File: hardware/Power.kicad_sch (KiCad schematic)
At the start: 33 parts, among them J200 Conn_Receptacle_2P, J201 Solder pad, J202 Solder pad, J203 Solder pad, J204 Solder pad, Q200 AO3401A, SW200 SW_Push_Dual, SW201 SW_Push_Dual, SW202 MU-AS90R, U200 RT9080-33GJ5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

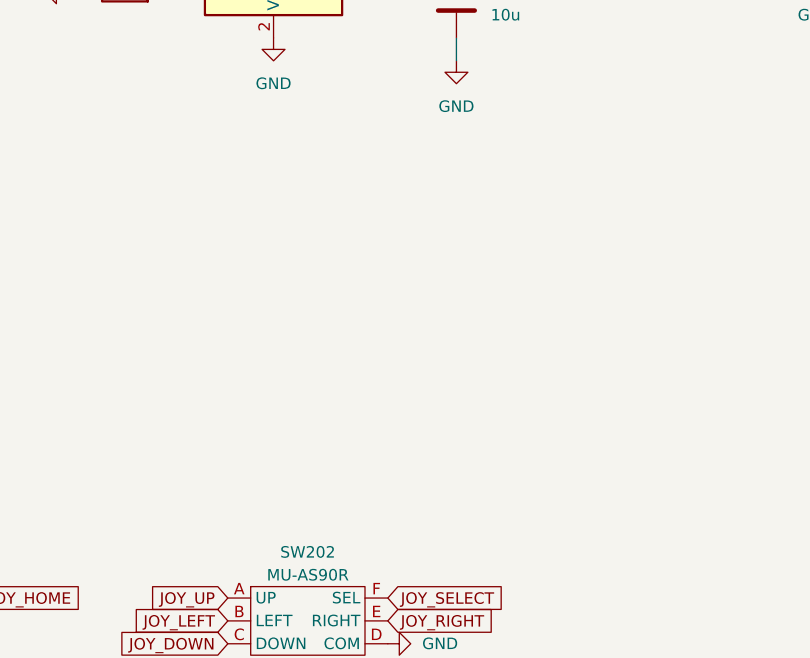
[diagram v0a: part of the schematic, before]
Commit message: Add crystal oscillator and hide designators from PCB
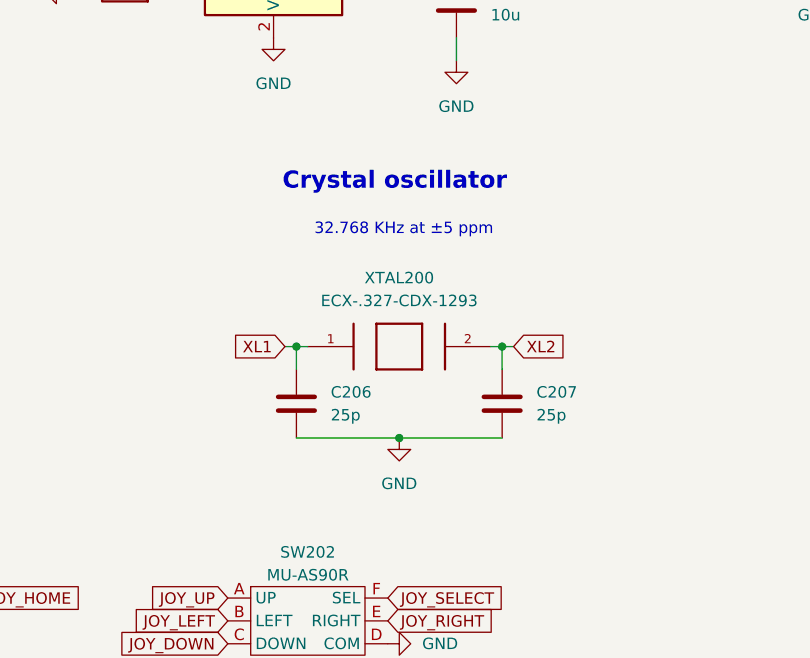
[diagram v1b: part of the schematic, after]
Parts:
- added C206, C207: 25p, Capacitor_SMD:C_0201_0603Metric_Pad0.64x0.40mm_HandSolder, symbol Device:C
- added XTAL200: ECX-.327-CDX-1293, ECX-.327-CDX-1293:XTAL_ECS-.327-12.5-34RR-TR, symbol ECX-.327-CDX-1293:ECX-.327-CDX-1293
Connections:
- net GND: now also C206.2, C207.2
- new net XL1: C206.1, XTAL200.1
- new net XL2: C207.1, XTAL200.2
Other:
- note added: "32.768 KHz at ±5 ppm"
- note added: "Crystal oscillator"

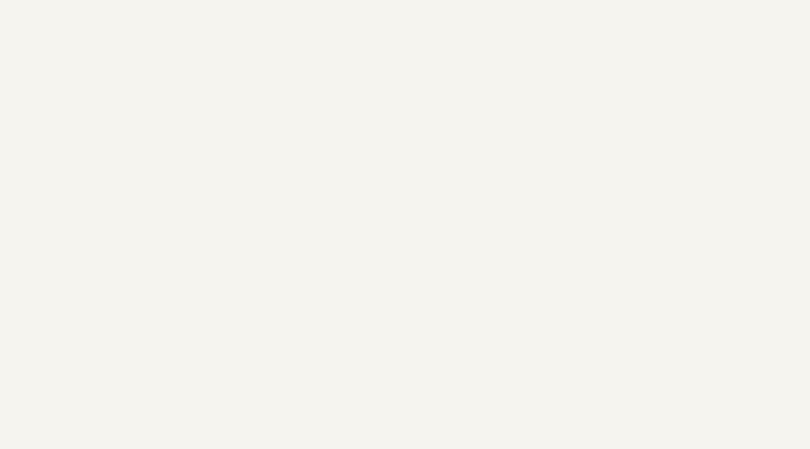
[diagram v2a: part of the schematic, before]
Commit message: Add mounting tabs to edges of PCB
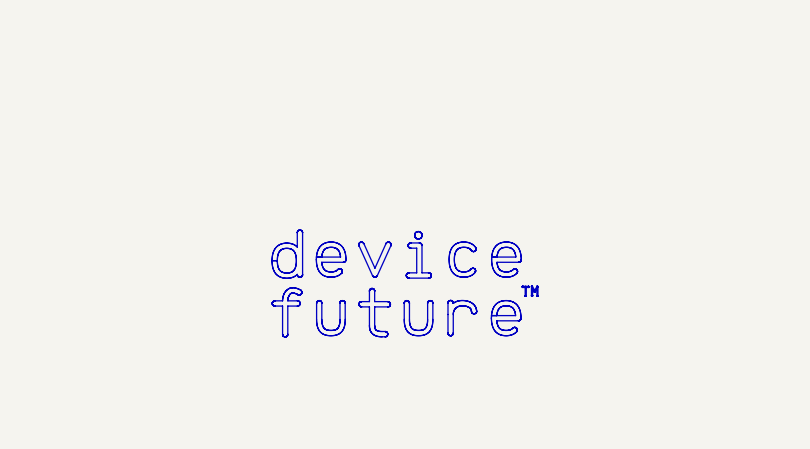
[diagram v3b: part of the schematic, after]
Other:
- company: (none) -> DeviceFuture
- title: (none) -> DigiCron

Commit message: Update PCB to use 0402 resistor/capacitor packages
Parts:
- C200, C201, C202, C203, C204, C205, C206, C207: footprint Capacitor_SMD:C_0201_0603Metric_Pad0.64x0.40mm_HandSolder -> Resistor_SMD:R_0402_1005Metric_Pad0.72x0.64mm_HandSolder
- R200, R201, R202, R203, R204, R205, R206, R207, R208, R209, R210: footprint Resistor_SMD:R_0201_0603Metric_Pad0.64x0.40mm_HandSolder -> Resistor_SMD:R_0402_1005Metric_Pad0.72x0.64mm_HandSolder
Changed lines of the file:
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@@
 			)
 		)
-		(property "Footprint" "Resistor_SMD:R_0201_0603Metric_Pad0.64x0.40mm_HandSolder"
+		(property "Footprint" "Resistor_SMD:R_0402_1005Metric_Pad0.72x0.64mm_HandSolder"
 			(at 123.952 63.5 90)
 			(effects
@@
 			)
 		)
-		(property "Footprint" "Capacitor_SMD:C_0201_0603Metric_Pad0.64x0.40mm_HandSolder"
+		(property "Footprint" "Resistor_SMD:R_0402_1005Metric_Pad0.72x0.64mm_HandSolder"
 			(at 260.35 47.2948 0)
 			(effects
@@
 			)
 		)
-		(property "Footprint" "Capacitor_SMD:C_0201_0603Metric_Pad0.64x0.40mm_HandSolder"
+		(property "Footprint" "Resistor_SMD:R_0402_1005Metric_Pad0.72x0.64mm_HandSolder"
 			(at 252.4252 123.19 0)
 			(effects
@@
 			)
 		)
-		(property "Footprint" "Capacitor_SMD:C_0201_0603Metric_Pad0.64x0.40mm_HandSolder"
+		(property "Footprint" "Resistor_SMD:R_0402_1005Metric_Pad0.72x0.64mm_HandSolder"
 			(at 192.7352 58.42 0)
 			(effects
@@
 			)
 		)
-		(property "Footprint" "Capacitor_SMD:C_0201_0603Metric_Pad0.64x0.40mm_HandSolder"
+		(property "Footprint" "Resistor_SMD:R_0402_1005Metric_Pad0.72x0.64mm_HandSolder"
 			(at 134.3152 120.65 0)
 			(effects
@@
 			)
 		)
-		(property "Footprint" "Resistor_SMD:R_0201_0603Metric_Pad0.64x0.40mm_HandSolder"
+		(property "Footprint" "Resistor_SMD:R_0402_1005Metric_Pad0.72x0.64mm_HandSolder"
 			(at 177.292 54.61 90)
 			(effects
@@
 			)
 		)
-		(property "Footprint" "Capacitor_SMD:C_0201_0603Metric_Pad0.64x0.40mm_HandSolder"
+		(property "Footprint" "Resistor_SMD:R_0402_1005Metric_Pad0.72x0.64mm_HandSolder"
 			(at 173.99 93.0148 0)
 			(effects
@@
 			)
 		)
-		(property "Footprint" "Resistor_SMD:R_0201_0603Metric_Pad0.64x0.40mm_HandSolder"
+		(property "Footprint" "Resistor_SMD:R_0402_1005Metric_Pad0.72x0.64mm_HandSolder"
 			(at 85.09 47.498 90)
 			(effects
@@
 			)
 		)
-		(property "Footprint" "Resistor_SMD:R_0201_0603Metric_Pad0.64x0.40mm_HandSolder"
+		(property "Footprint" "Resistor_SMD:R_0402_1005Metric_Pad0.72x0.64mm_HandSolder"
 			(at 38.1 83.058 90)
 			(effects
@@
 			)
 		)
-		(property "Footprint" "Resistor_SMD:R_0201_0603Metric_Pad0.64x0.40mm_HandSolder"
+		(property "Footprint" "Resistor_SMD:R_0402_1005Metric_Pad0.72x0.64mm_HandSolder"
 			(at 38.1 77.978 90)
 			(effects
@@
 			)
 		)
-		(property "Footprint" "Capacitor_SMD:C_0201_0603Metric_Pad0.64x0.40mm_HandSolder"
+		(property "Footprint" "Resistor_SMD:R_0402_1005Metric_Pad0.72x0.64mm_HandSolder"
 			(at 139.3952 165.1 0)
 			(effects
@@
 			)
 		)
-		(property "Footprint" "Resistor_SMD:R_0201_0603Metric_Pad0.64x0.40mm_HandSolder"
+		(property "Footprint" "Resistor_SMD:R_0402_1005Metric_Pad0.72x0.64mm_HandSolder"
 			(at 241.3 59.182 90)
 			(effects
@@
 			)
 		)
-		(property "Footprint" "Resistor_SMD:R_0201_0603Metric_Pad0.64x0.40mm_HandSolder"
+		(property "Footprint" "Resistor_SMD:R_0402_1005Metric_Pad0.72x0.64mm_HandSolder"
 			(at 224.282 128.27 90)
 			(effects
@@
 			)
 		)
-		(property "Footprint" "Resistor_SMD:R_0201_0603Metric_Pad0.64x0.40mm_HandSolder"
+		(property "Footprint" "Resistor_SMD:R_0402_1005Metric_Pad0.72x0.64mm_HandSolder"
 			(at 96.52 117.348 90)
 			(effects
@@
 			)
 		)
-		(property "Footprint" "Resistor_SMD:R_0201_0603Metric_Pad0.64x0.40mm_HandSolder"
+		(property "Footprint" "Resistor_SMD:R_0402_1005Metric_Pad0.72x0.64mm_HandSolder"
 			(at 123.952 50.8 90)
 			(effects
@@
 			)
 		)
-		(property "Footprint" "Resistor_SMD:R_0201_0603Metric_Pad0.64x0.40mm_HandSolder"
+		(property "Footprint" "Resistor_SMD:R_0402_1005Metric_Pad0.72x0.64mm_HandSolder"
 			(at 224.282 118.11 90)
 			(effects
@@
 			)
 		)
-		(property "Footprint" "Capacitor_SMD:C_0201_0603Metric_Pad0.64x0.40mm_HandSolder"
+		(property "Footprint" "Resistor_SMD:R_0402_1005Metric_Pad0.72x0.64mm_HandSolder"
 			(at 239.7252 123.19 0)
 			(effects
@@
 			)
 		)
-		(property "Footprint" "Capacitor_SMD:C_0201_0603Metric_Pad0.64x0.40mm_HandSolder"
+		(property "Footprint" "Resistor_SMD:R_0402_1005Metric_Pad0.72x0.64mm_HandSolder"
 			(at 116.5352 165.1 0)
 			(effects
@@
 			)
 		)
-		(property "Footprint" "Resistor_SMD:R_0201_0603Metric_Pad0.64x0.40mm_HandSolder"
+		(property "Footprint" "Resistor_SMD:R_0402_1005Metric_Pad0.72x0.64mm_HandSolder"
 			(at 77.47 44.958 90)
 			(effects

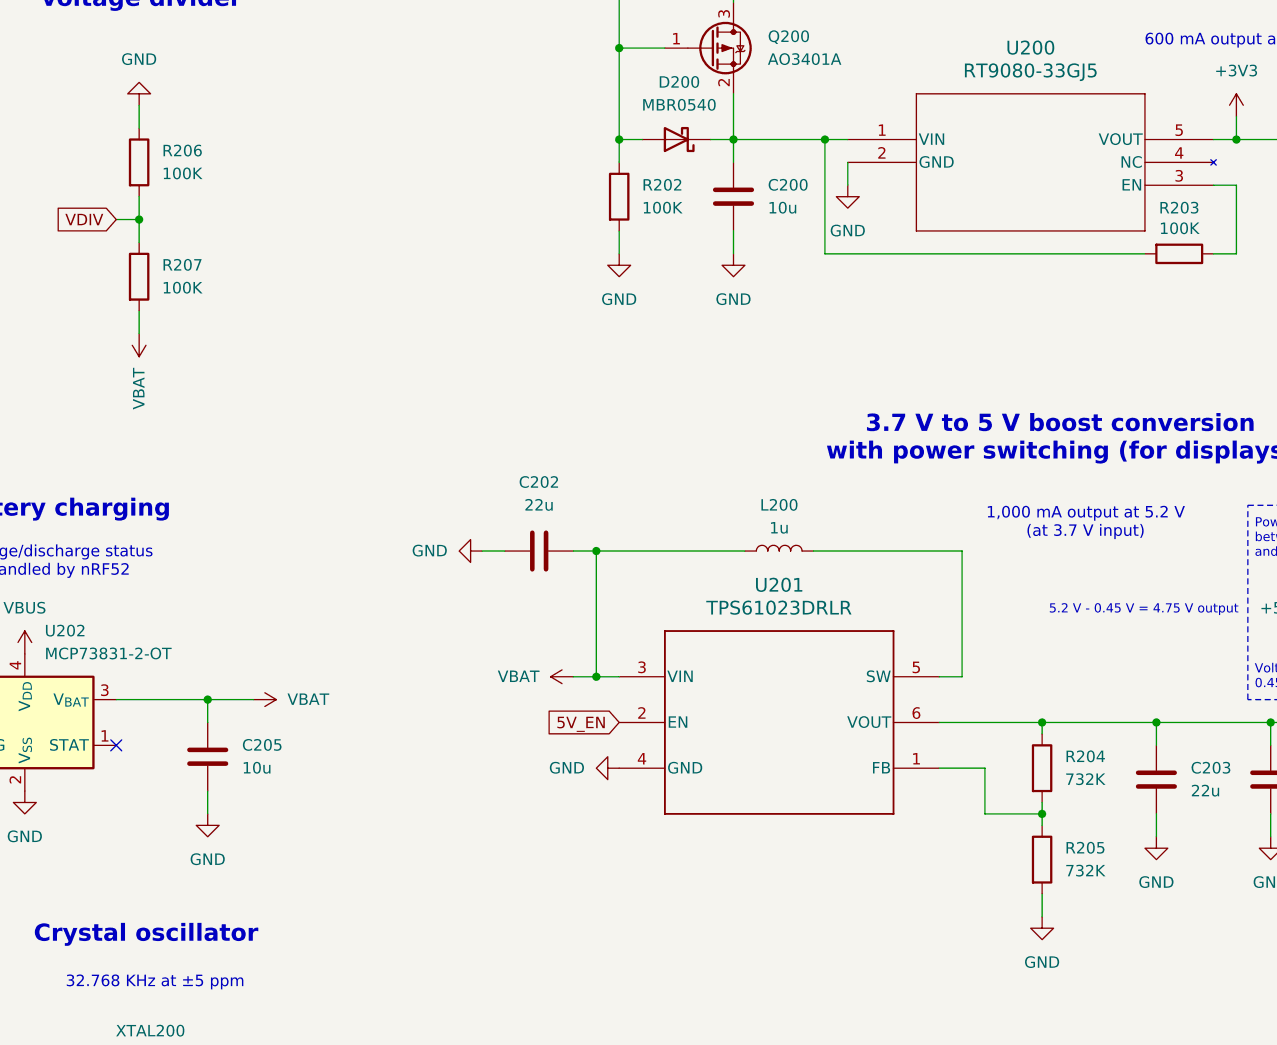
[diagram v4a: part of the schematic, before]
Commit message: Fix a few resistor values on PCB relating to power management
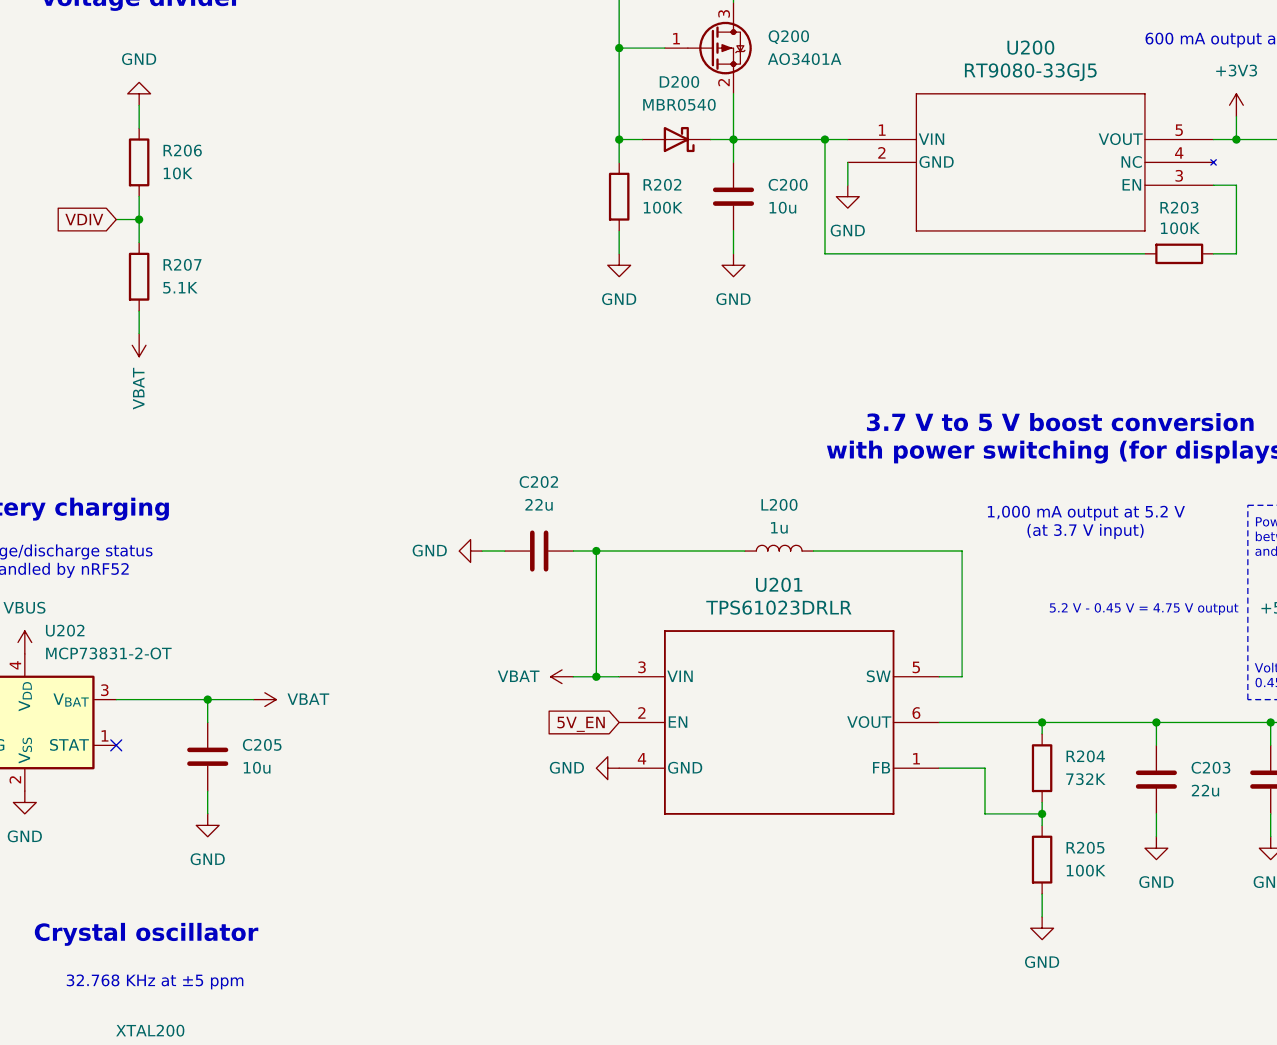
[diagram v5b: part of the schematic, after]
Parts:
- R205: value 732K -> 100K
- R206: value 100K -> 10K
- R207: value 100K -> 5.1K
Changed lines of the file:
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@@
 			)
 		)
-		(property "Value" "100K"
+		(property "Value" "5.1K"
 			(at 128.27 64.7699 0)
 			(effects
@@
 			)
 		)
-		(property "Value" "732K"
+		(property "Value" "100K"
 			(at 228.6 129.5399 0)
 			(effects
@@
 			)
 		)
-		(property "Value" "100K"
+		(property "Value" "10K"
 			(at 128.27 52.0699 0)
 			(effects

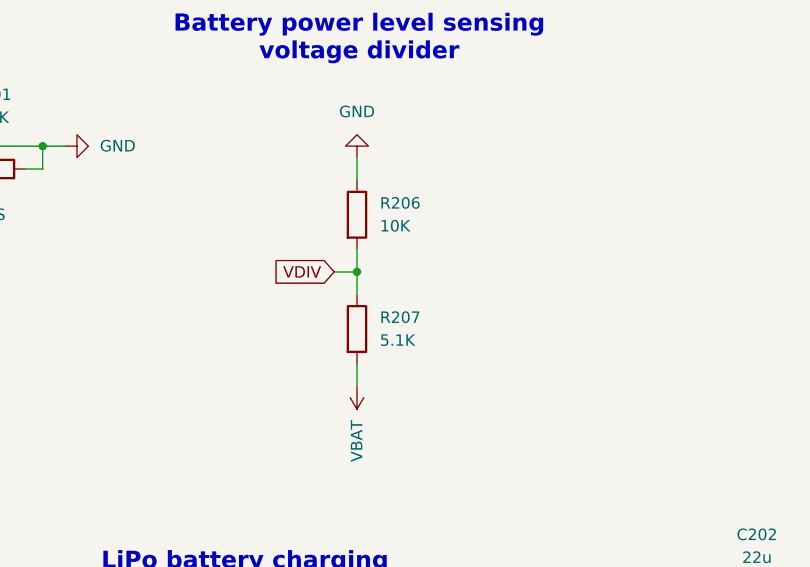
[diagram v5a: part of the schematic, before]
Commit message: Make a few changes to footprint selection and resistor/capacitor values
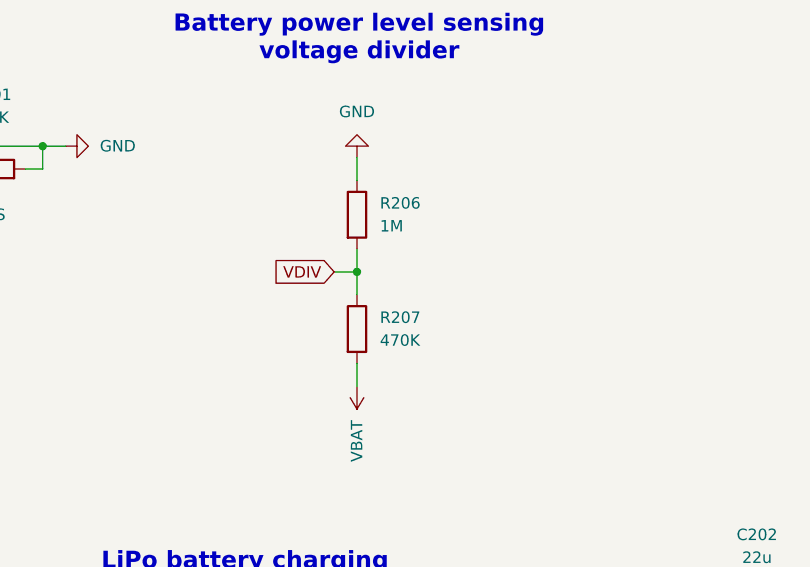
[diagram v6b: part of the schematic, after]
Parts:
- C200, C201, C202, C203, C204, C205, C206, C207: footprint Resistor_SMD:R_0402_1005Metric_Pad0.72x0.64mm_HandSolder -> Capacitor_SMD:C_0402_1005Metric_Pad0.74x0.62mm_HandSolder
- R206: value 10K -> 1M
- R207: value 5.1K -> 470K
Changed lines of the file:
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@@
 			)
 		)
-		(property "Value" "5.1K"
+		(property "Value" "470K"
 			(at 128.27 64.7699 0)
 			(effects
@@
 			)
 		)
-		(property "Footprint" "Resistor_SMD:R_0402_1005Metric_Pad0.72x0.64mm_HandSolder"
+		(property "Footprint" "Capacitor_SMD:C_0402_1005Metric_Pad0.74x0.62mm_HandSolder"
 			(at 260.35 47.2948 0)
 			(effects
@@
 			)
 		)
-		(property "Footprint" "Resistor_SMD:R_0402_1005Metric_Pad0.72x0.64mm_HandSolder"
+		(property "Footprint" "Capacitor_SMD:C_0402_1005Metric_Pad0.74x0.62mm_HandSolder"
 			(at 252.4252 123.19 0)
 			(effects
@@
 			)
 		)
-		(property "Footprint" "Resistor_SMD:R_0402_1005Metric_Pad0.72x0.64mm_HandSolder"
+		(property "Footprint" "Capacitor_SMD:C_0402_1005Metric_Pad0.74x0.62mm_HandSolder"
 			(at 192.7352 58.42 0)
 			(effects
@@
 			)
 		)
-		(property "Footprint" "Resistor_SMD:R_0402_1005Metric_Pad0.72x0.64mm_HandSolder"
+		(property "Footprint" "Capacitor_SMD:C_0402_1005Metric_Pad0.74x0.62mm_HandSolder"
 			(at 134.3152 120.65 0)
 			(effects
@@
 			)
 		)
-		(property "Footprint" "Resistor_SMD:R_0402_1005Metric_Pad0.72x0.64mm_HandSolder"
+		(property "Footprint" "Capacitor_SMD:C_0402_1005Metric_Pad0.74x0.62mm_HandSolder"
 			(at 173.99 93.0148 0)
 			(effects
@@
 			)
 		)
-		(property "Footprint" "Resistor_SMD:R_0402_1005Metric_Pad0.72x0.64mm_HandSolder"
+		(property "Footprint" "Capacitor_SMD:C_0402_1005Metric_Pad0.74x0.62mm_HandSolder"
 			(at 139.3952 165.1 0)
 			(effects
@@
 			)
 		)
-		(property "Value" "10K"
+		(property "Value" "1M"
 			(at 128.27 52.0699 0)
 			(effects
@@
 			)
 		)
-		(property "Footprint" "Resistor_SMD:R_0402_1005Metric_Pad0.72x0.64mm_HandSolder"
+		(property "Footprint" "Capacitor_SMD:C_0402_1005Metric_Pad0.74x0.62mm_HandSolder"
 			(at 239.7252 123.19 0)
 			(effects
@@
 			)
 		)
-		(property "Footprint" "Resistor_SMD:R_0402_1005Metric_Pad0.72x0.64mm_HandSolder"
+		(property "Footprint" "Capacitor_SMD:C_0402_1005Metric_Pad0.74x0.62mm_HandSolder"
 			(at 116.5352 165.1 0)
 			(effects

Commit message: Fix pin routing for battery power level sensing
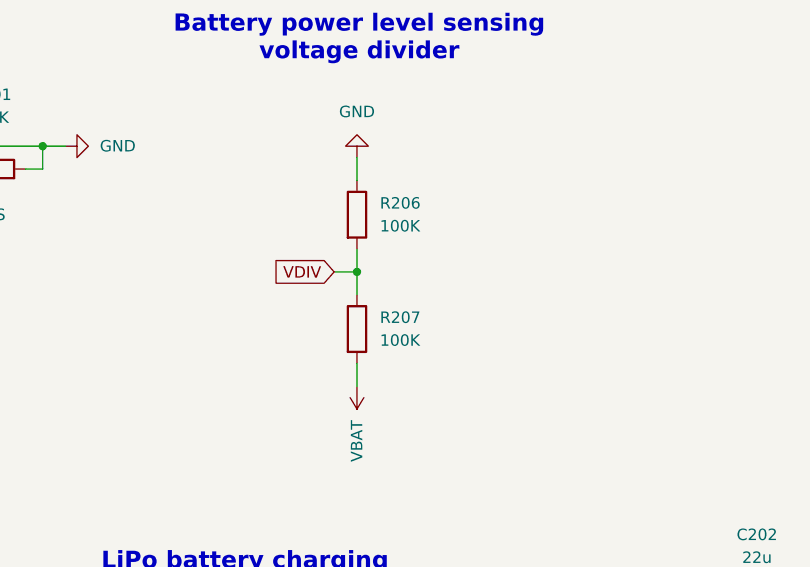
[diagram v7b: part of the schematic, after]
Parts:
- R206: value 1M -> 100K
- R207: value 470K -> 100K
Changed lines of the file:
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@@
 			)
 		)
-		(property "Value" "470K"
+		(property "Value" "100K"
 			(at 128.27 64.7699 0)
 			(effects
@@
 			)
 		)
-		(property "Value" "1M"
+		(property "Value" "100K"
 			(at 128.27 52.0699 0)
 			(effects
